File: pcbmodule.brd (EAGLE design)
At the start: 105 x 82 mm, 13 parts, among them X11 MKDSN1,5/6-5,08, X5 MKDSN1,5/6-5,08, X8 MKDSN1,5/10-5,08, X9 MKDSN1,5/10-5,08

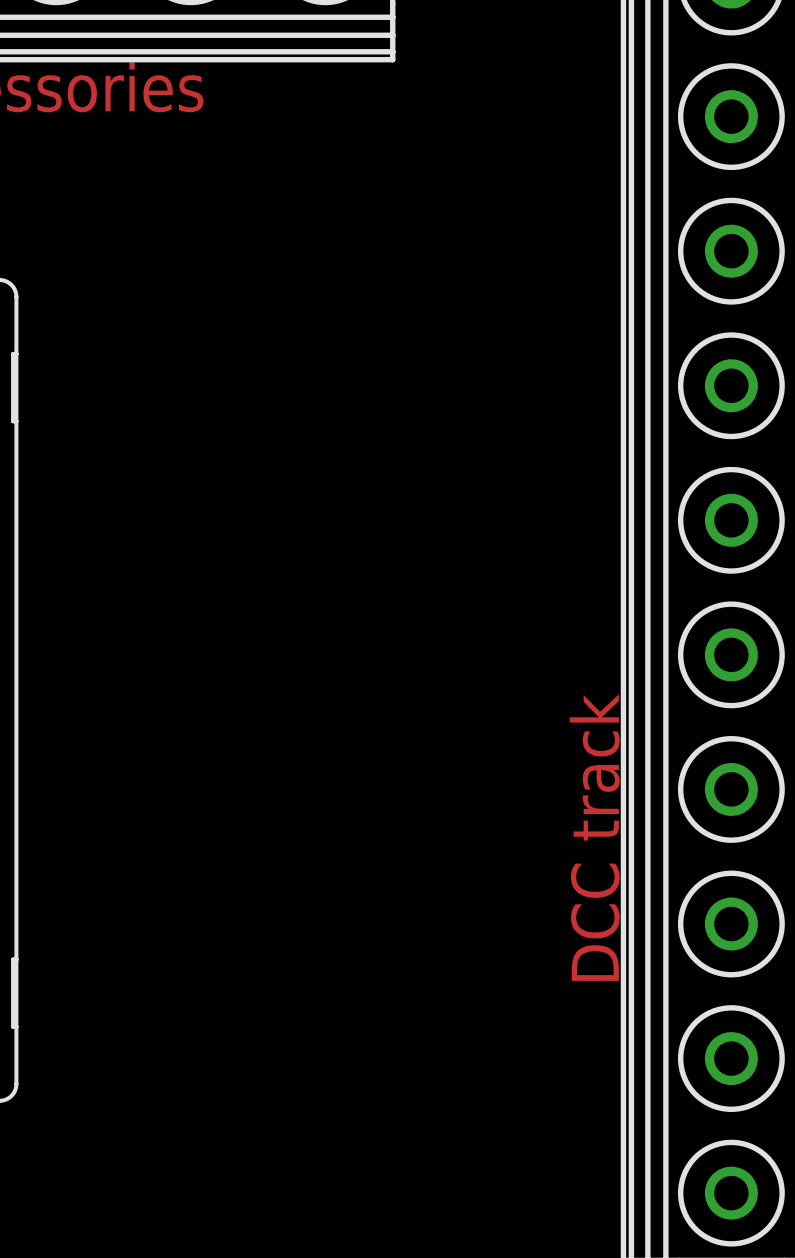
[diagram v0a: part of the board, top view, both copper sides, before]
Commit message: add led indicator (bipolar red/green led: http://www.ledsales.com.au/index.php?main_page=product_info&products_id=1683)
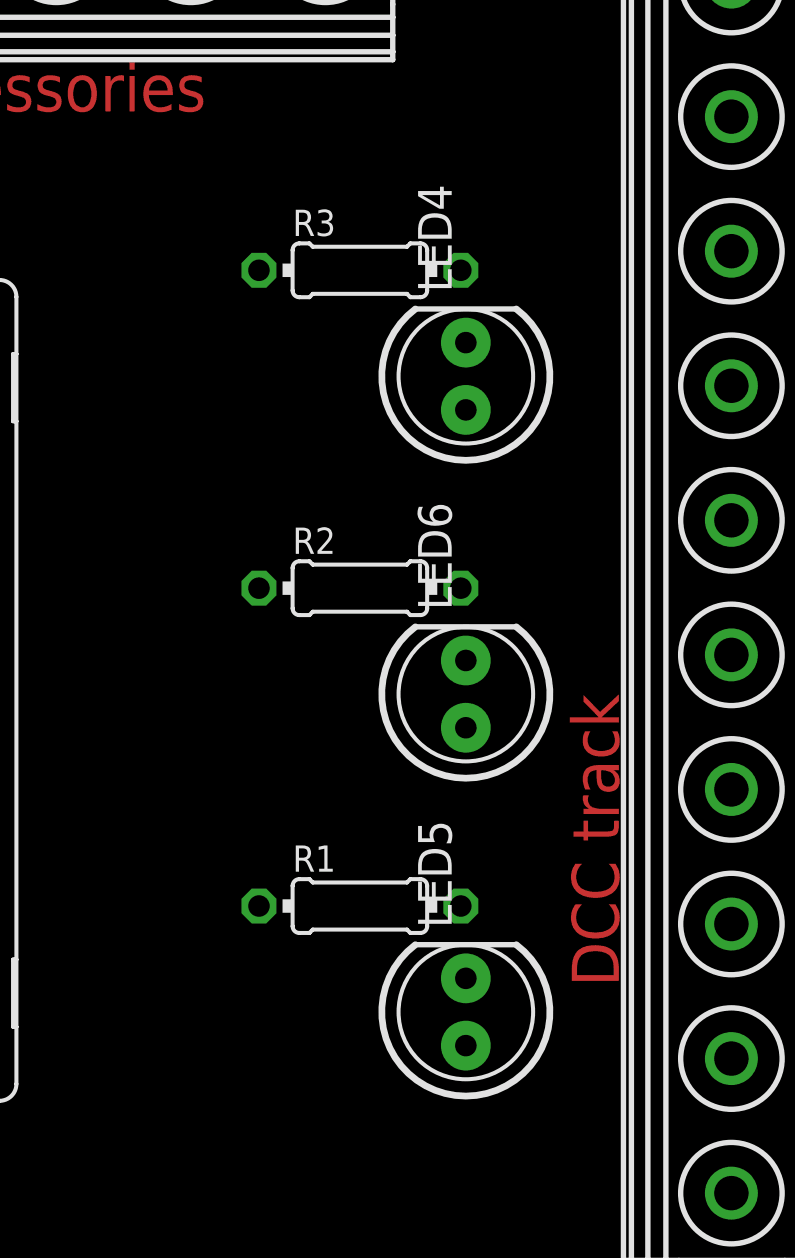
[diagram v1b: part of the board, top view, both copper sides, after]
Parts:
- added LED4, LED5, LED6: (no value), SparkFun-LED:LED5MM
- added R1, R2, R3: 2.5k, resistor:0204/7
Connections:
- new net N$15: LED5.K, R1.2
- new net N$16: LED6.K, R2.2
- new net N$5: LED4.K, R3.2
- net N$1: now also R3.1
- net N$14: now also LED6.A
- net N$17: now also R2.1
- net N$2: now also LED4.A
- net N$4: now also R1.1
- net N$6: now also LED5.A

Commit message: update schema for proper RJ45 module layout
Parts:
- removed U$6: RJ45-TRAFO-L, con-amphenol-rj45-ld:RJ45-TRAFO-L
- added U$4: RJ45-TRAFO, con-amphenol-rj45-nzin:RJ45-RJHSE5E8X
- U$1, U$2, U$3, U$5: value RJ45-TRAFO-L -> RJ45-TRAFO; device con-amphenol-rj45-ld:RJ45-TRAFO-L -> con-amphenol-rj45-nzin:RJ45-RJHSE5E8X
- moved U$5 60.0 mm to (92.0, 12.0), turned to 0 degrees
- moved U$1 58.0 mm to (12.0, 12.0), turned to 0 degrees
- moved U$2 58.0 mm to (32.0, 12.0), turned to 0 degrees
- moved U$3 2.24 mm to (52.0, 12.0), turned to 0 degrees
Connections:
- removed net GND1: U$1.GND1, U$2.GND1, U$3.GND1, U$5.GND1, U$6.GND1
- removed net GND2: U$1.GND2, U$2.GND2, U$3.GND2, U$5.GND2, U$6.GND2
- removed net N$10: U$1.5, U$2.5, U$3.5, U$5.5, U$6.5
- removed net N$11: U$1.6, U$2.6, U$3.6, U$5.6, U$6.6
- removed net N$12: U$1.7, U$2.7, U$3.7, U$5.7, U$6.7
- removed net N$13: U$1.8, U$2.8, U$3.8, U$5.8, U$6.8
- removed net N$3: U$1.1, U$2.1, U$3.1, U$5.1, U$6.1
- removed net N$7: U$1.2, U$2.2, U$3.2, U$5.2, U$6.2
- removed net N$8: U$1.3, U$2.3, U$3.3, U$5.3, U$6.3
- removed net N$9: U$1.4, U$2.4, U$3.4, U$5.4, U$6.4
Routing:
- net N$17: track 0.00 -> 281.8 mm
- net N$14: track 0.00 -> 222.1 mm, vias 0 -> 2
- net N$4: track 0.00 -> 181.7 mm
- net N$6: track 0.00 -> 165.8 mm
- net N$58: track 0.00 -> 135.0 mm, vias 0 -> 5
- net N$2: track 0.00 -> 131.5 mm
- net N$41: track 0.00 -> 125.0 mm, vias 0 -> 5
- net N$38: track 0.00 -> 120.0 mm, vias 0 -> 5
- net N$1: track 0.00 -> 116.5 mm
- net N$56: track 0.00 -> 115.0 mm, vias 0 -> 5
- net N$21: track 0.00 -> 110.0 mm, vias 0 -> 5
- net N$39: track 0.00 -> 105.0 mm, vias 0 -> 5
- net N$36: track 0.00 -> 100.0 mm, vias 0 -> 5
- net N$13: track 0.00 -> 90.0 mm, vias 0 -> 5
- net N$19: track 0.00 -> 77.3 mm
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
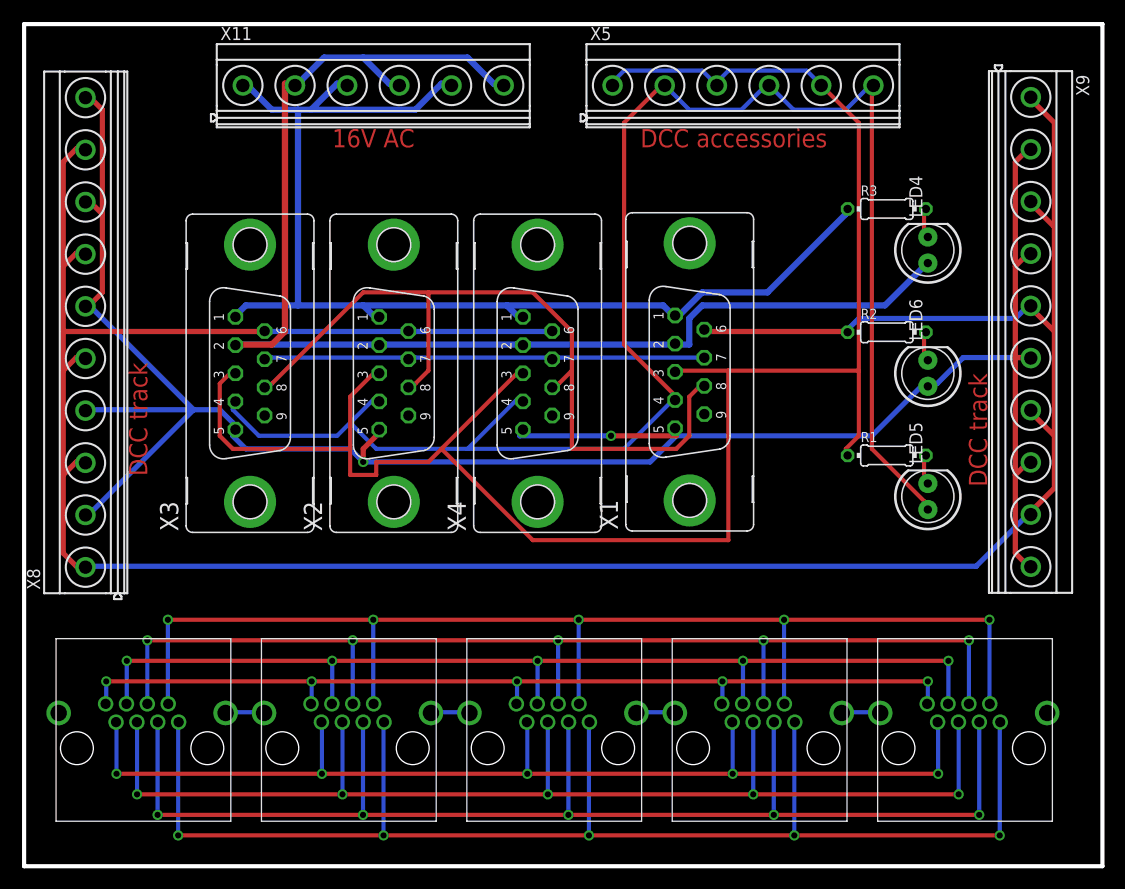
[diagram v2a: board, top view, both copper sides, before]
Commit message: reduce the size to 10 cm wide
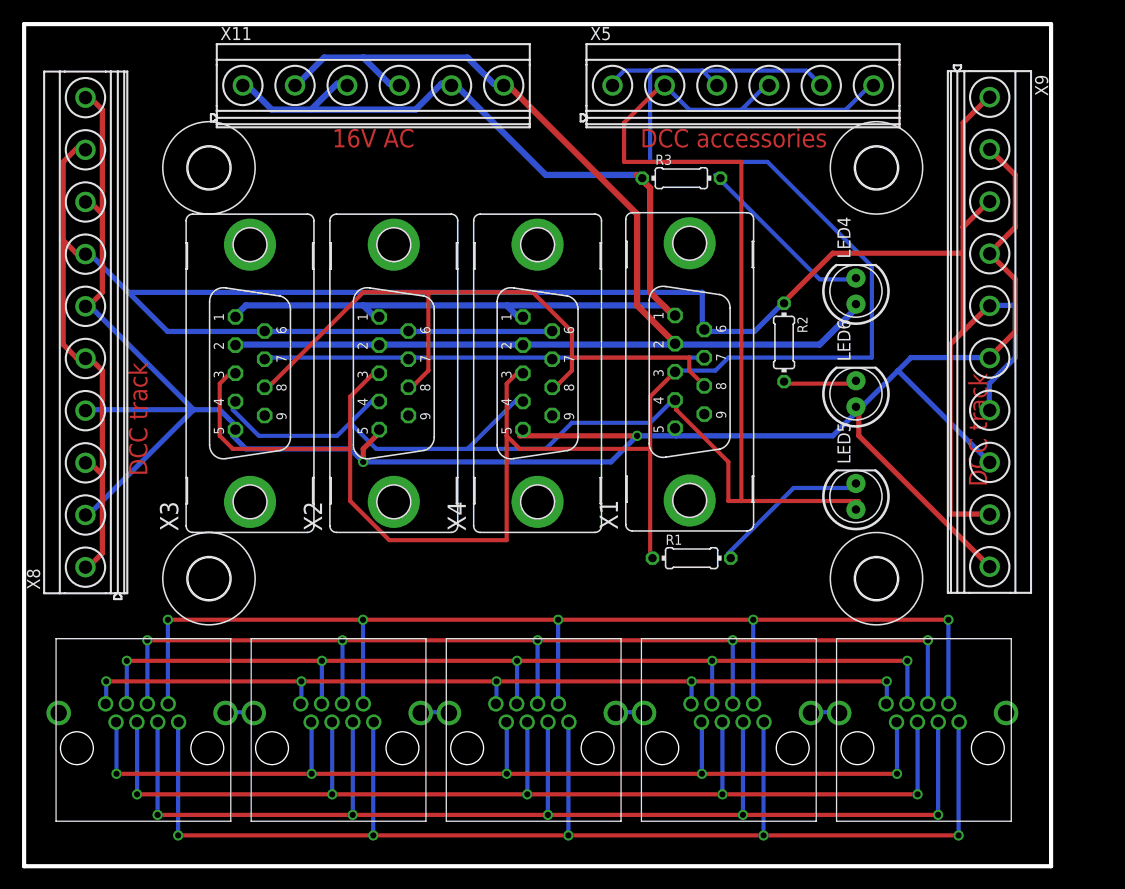
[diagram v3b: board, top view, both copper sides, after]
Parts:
- added U$6, U$7, U$8, U$9: (no value), holes:4,1
- moved R1 21.5 mm to (65.0, 30.0)
- moved R3 20.2 mm to (64.0, 67.0)
- moved R2 10.0 mm to (74.0, 51.0), turned to 270 degrees
- moved LED4 8.06 mm to (81.0, 56.0)
- moved LED6 7.28 mm to (81.0, 46.0)
- moved LED5 7.00 mm to (81.0, 36.0)
- moved U$5 4.00 mm to (88.0, 12.0)
- moved X9 4.00 mm to (94.0, 52.0)
- moved U$4 3.00 mm to (69.0, 12.0)
- moved U$3 2.00 mm to (50.0, 12.0)
- moved U$2 1.00 mm to (31.0, 12.0)
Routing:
- net N$58: track 135.0 -> 0.00 mm, vias 5 -> 0
- net N$23: track 0.00 -> 131.0 mm, vias 0 -> 5
- net N$41: track 125.0 -> 0.00 mm, vias 5 -> 0
- net N$55: track 0.00 -> 116.0 mm, vias 0 -> 5
- net N$56: track 115.0 -> 0.00 mm, vias 5 -> 0
- net N$12: track 0.00 -> 106.0 mm, vias 0 -> 5
- net N$39: track 105.0 -> 0.00 mm, vias 5 -> 0
- net N$53: track 0.00 -> 96.0 mm, vias 0 -> 5
- net N$13: track 90.0 -> 0.00 mm, vias 5 -> 0
- net N$10: track 0.00 -> 86.0 mm, vias 0 -> 5
- net N$17: track 281.8 -> 255.5 mm
- net N$5: track 3.55 -> 19.1 mm
- net N$15: track 2.83 -> 16.4 mm
- net N$19: track 77.3 -> 66.6 mm
- net N$4: track 181.7 -> 190.1 mm
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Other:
- board size 105 x 82 mm -> 100 x 82 mm

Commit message: Make some space to be able to plugin connector in an easier way
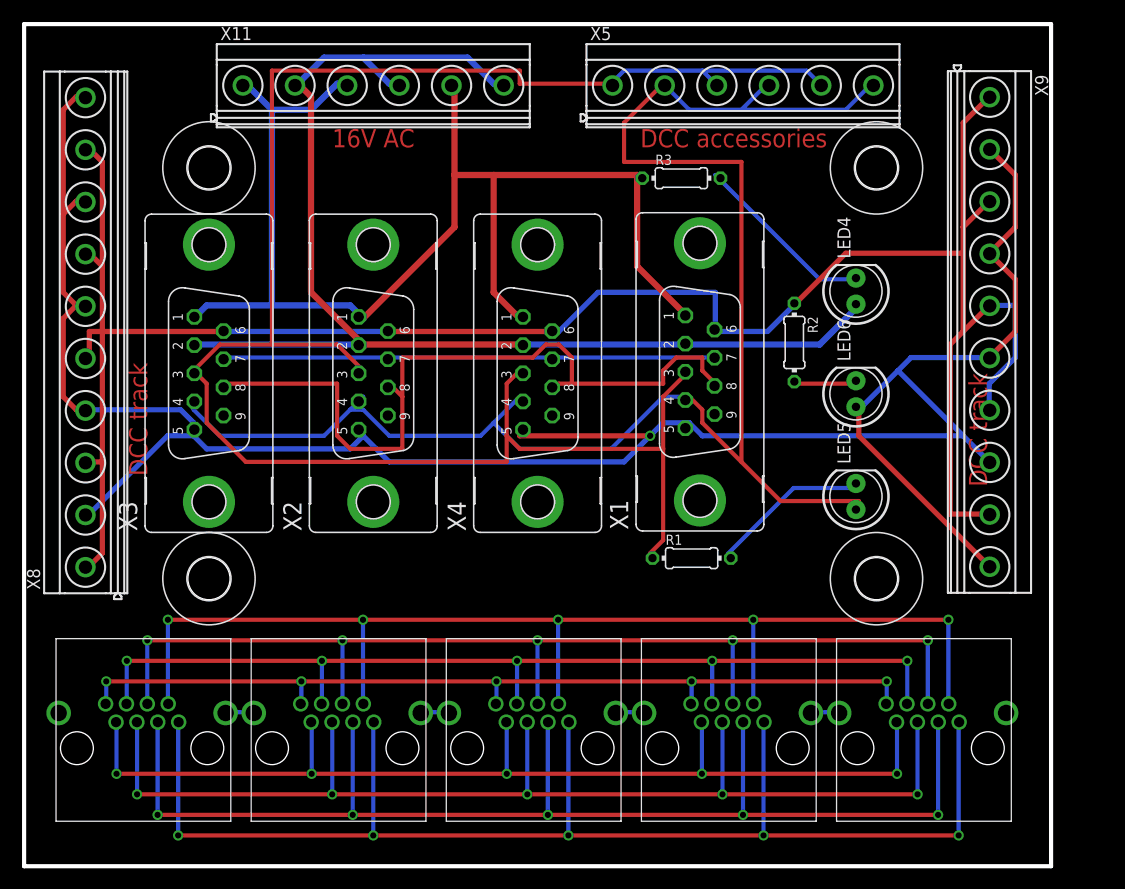
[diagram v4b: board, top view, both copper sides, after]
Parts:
- moved X3 4.00 mm to (18.0, 48.0)
- moved X2 2.00 mm to (34.0, 48.0)
- moved R2 1.00 mm to (75.0, 51.0)
- moved X1 1.00 mm to (65.8, 48.1)
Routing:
- net N$17: track 255.5 -> 211.9 mm
- net N$1: track 115.0 -> 127.2 mm
- net N$19: track 66.6 -> 74.9 mm
- net N$14: track 224.4 -> 231.5 mm, vias 2 -> 1
- net N$18: track 42.9 -> 49.0 mm
- net N$6: track 168.7 -> 163.5 mm
- net N$4: track 190.1 -> 186.7 mm
- net N$16: track 8.41 -> 6.96 mm

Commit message: - change spec for rj12 (instead of rj45) - add a 4th circuit line for (analogic) metric n lines
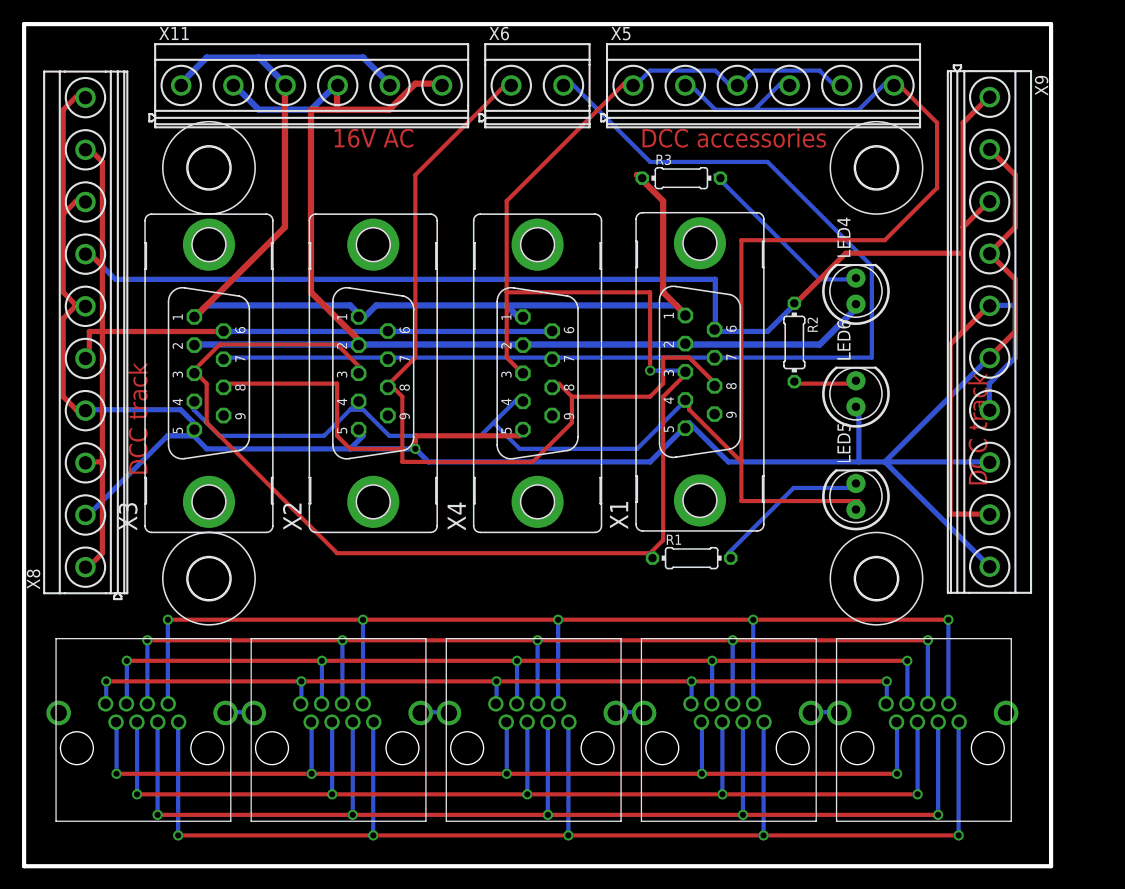
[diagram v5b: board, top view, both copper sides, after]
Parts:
- added X6: MKDSN1,5/2-5,08, con-phoenix-508:MKDSN1,5/2-5,08
- moved X11 6.00 mm to (28.0, 76.0)
- moved X5 2.00 mm to (72.0, 76.0)
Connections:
- net N$18: now also X6.2
- net N$19: now also X6.1
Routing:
- net N$18: track 49.0 -> 110.5 mm
- net N$17: track 211.9 -> 257.9 mm
- net N$19: track 74.9 -> 108.4 mm
- net N$14: track 231.5 -> 220.2 mm
- net N$4: track 186.7 -> 176.6 mm, vias 0 -> 1
- net N$6: track 163.5 -> 170.9 mm
- net N$1: track 127.2 -> 124.2 mm
- net N$2: track 124.1 -> 122.6 mm
